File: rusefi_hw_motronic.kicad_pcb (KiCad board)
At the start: 2 copper layers, 175 x 129 mm, 43 parts, among them J1 OMEGA PCC_SMP_K, J2 Conn_01x02_Female, Q1 ZXTN2040, U1 SFH617A-2X009T, U2 BOSCH_55P, U3 molex_48pin_MRE, U4 MAX31855KASA, U5 TPIC8101, U6 MPXA4250A6U, U7 TE_6437288-6

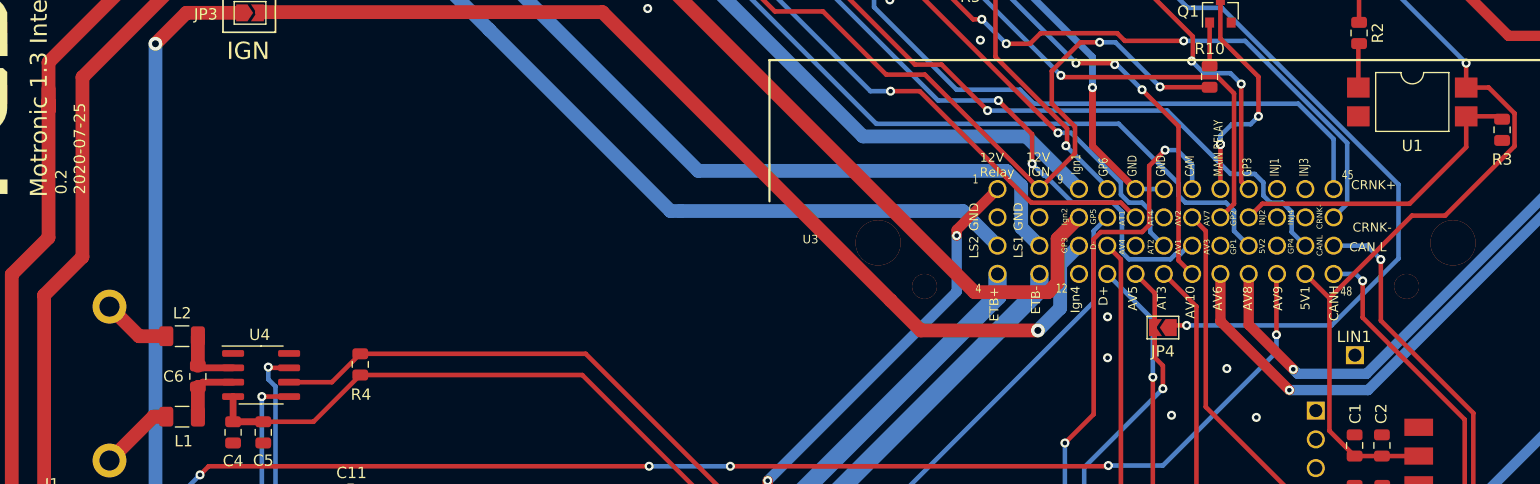
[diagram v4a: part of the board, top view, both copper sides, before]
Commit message: added PPS pins
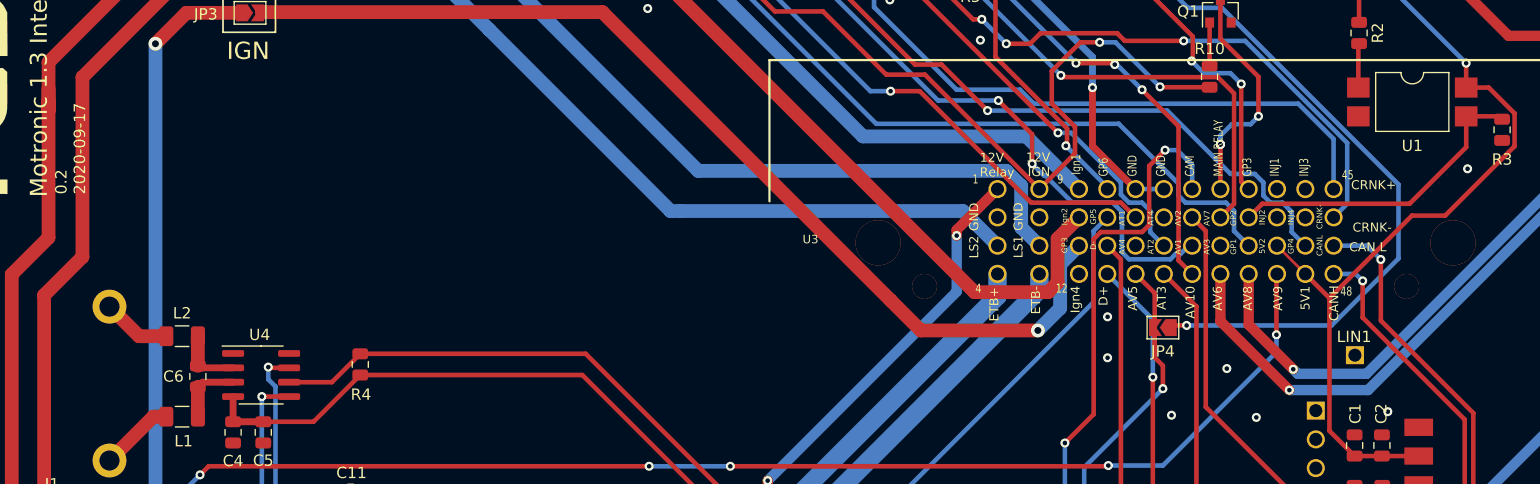
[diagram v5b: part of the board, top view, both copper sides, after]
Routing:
- net +5V: track 277.8 -> 281.3 mm
- net GND: vias 30 -> 32
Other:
- board text added: "0.2 2020-09-17"
- board text removed: "0.2 2020-07-25"

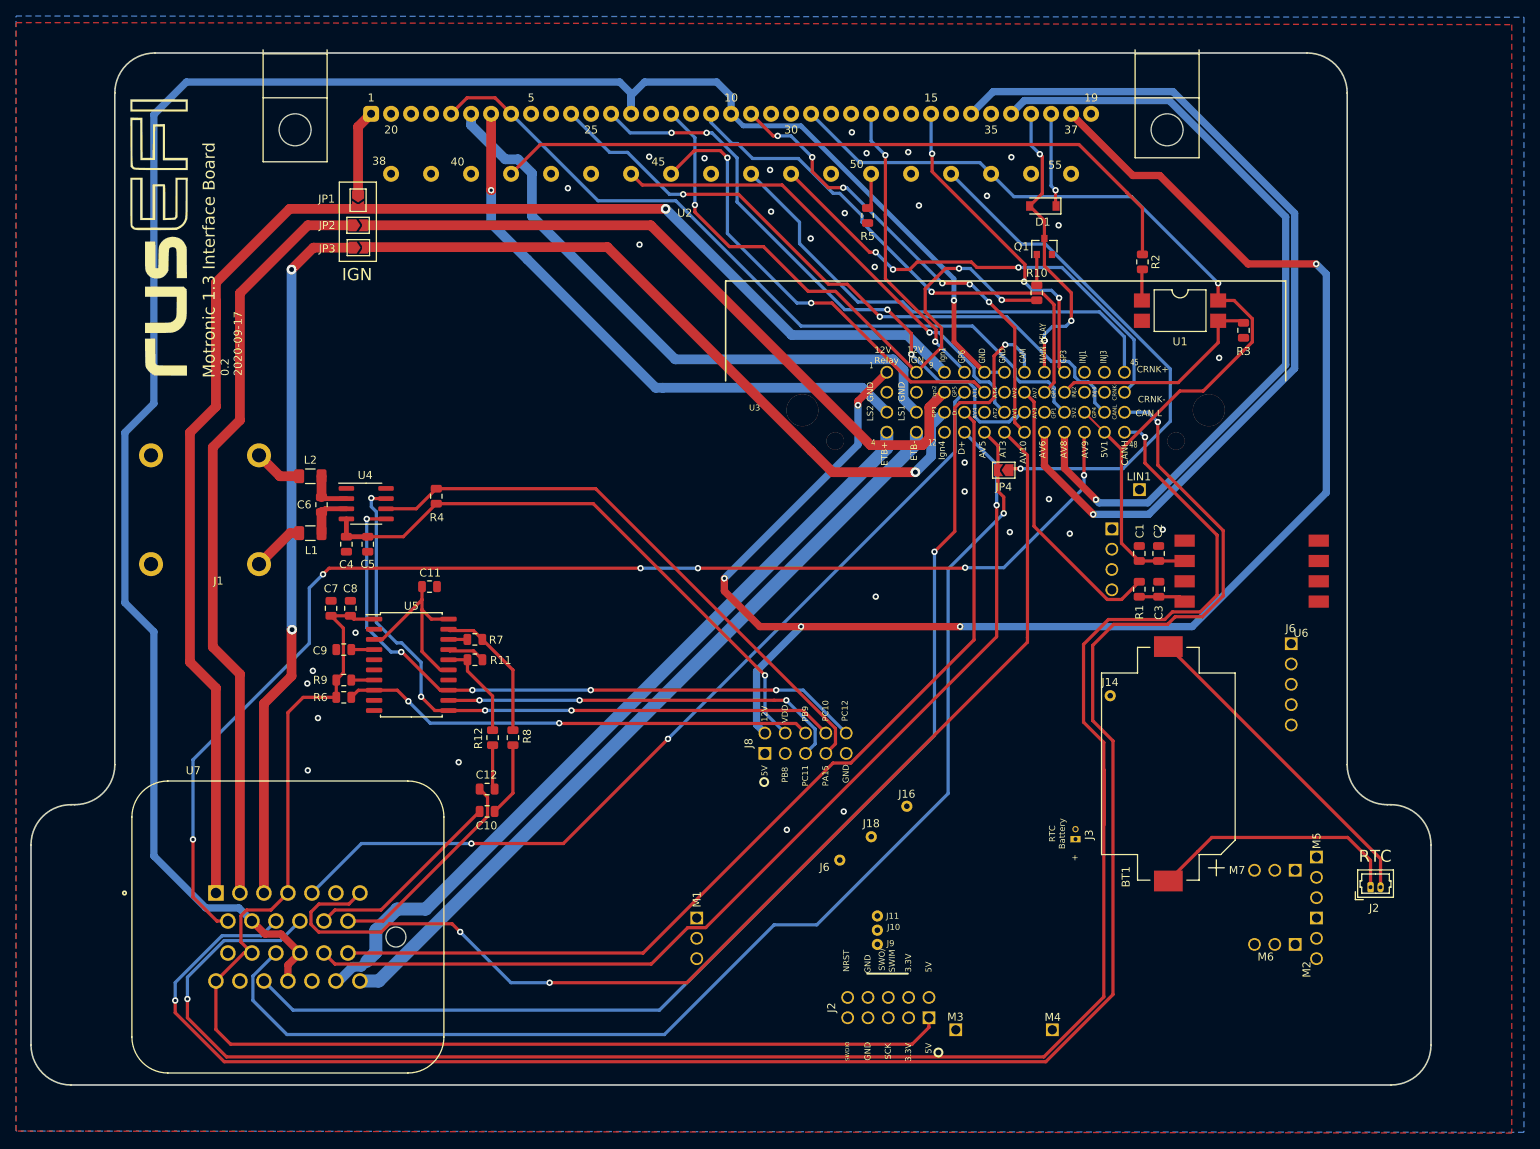
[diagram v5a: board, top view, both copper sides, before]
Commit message: added etb sensor pins to layout
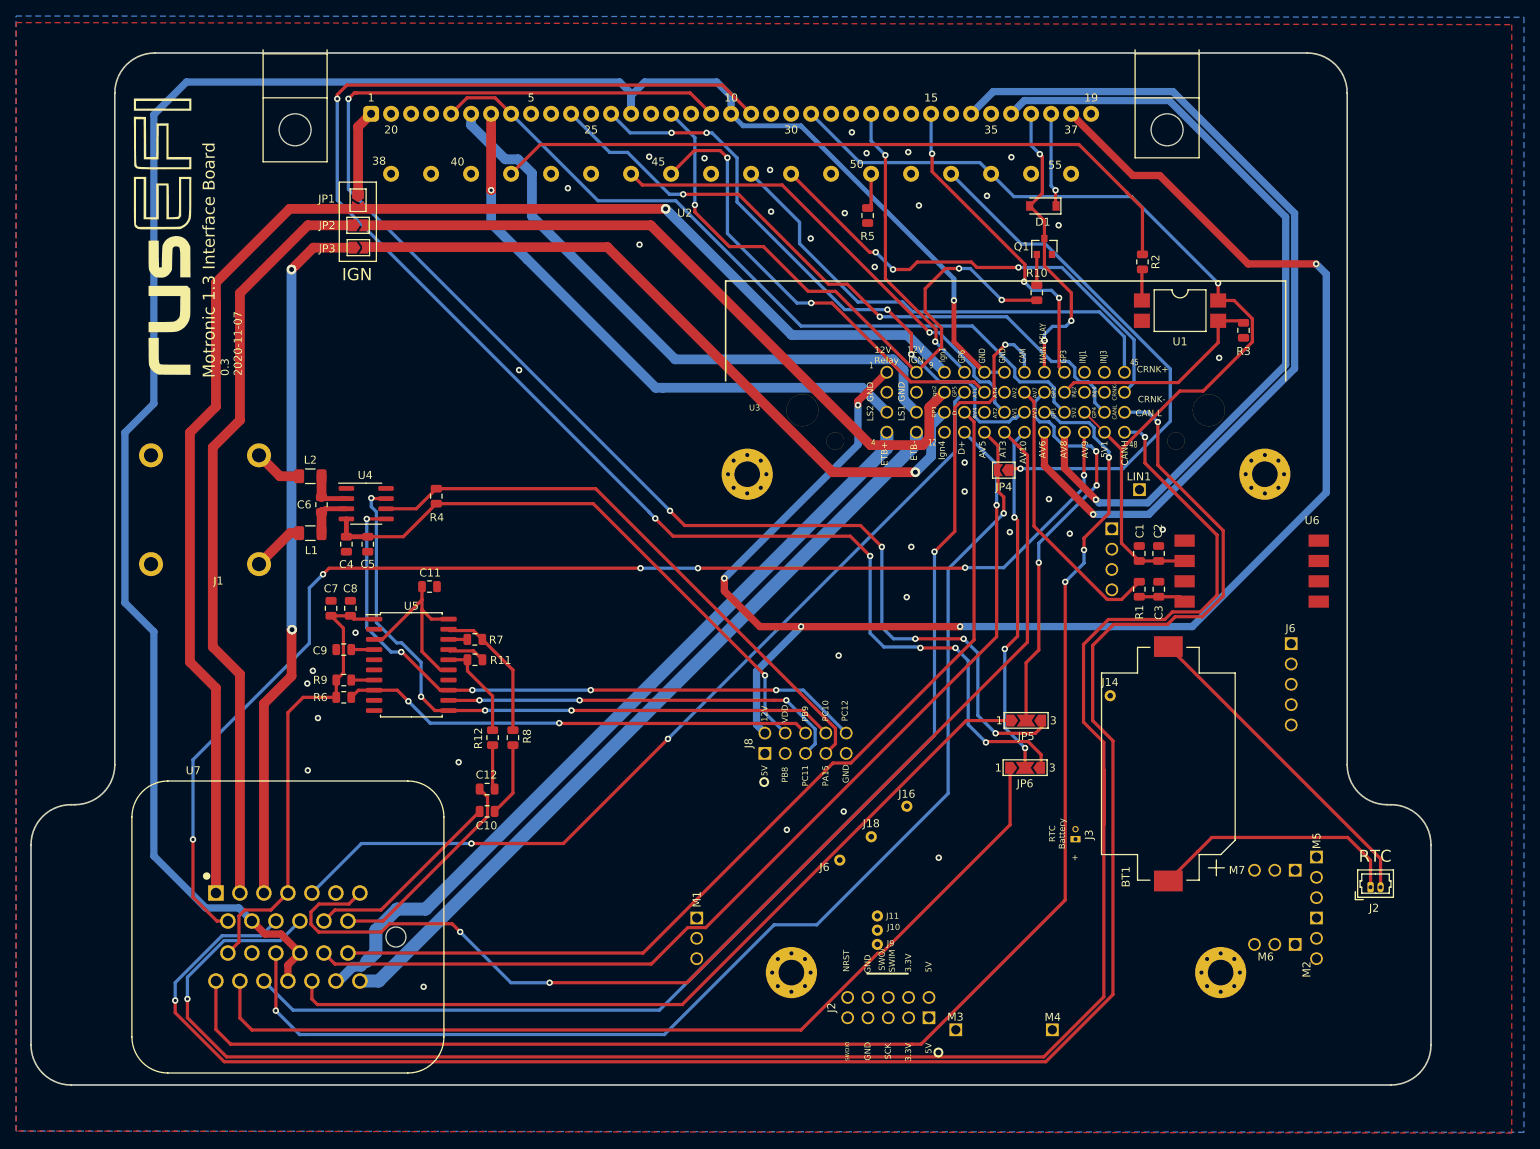
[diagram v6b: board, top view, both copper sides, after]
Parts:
- added JP5: SolderJumper_3_Open, Jumper:SolderJumper-3_P2.0mm_Open_TrianglePad1.0x1.5mm_NumberLabels, F.Cu at (147.6, 111.2)
- added JP6: SolderJumper_3_Open, Jumper:SolderJumper-3_P2.0mm_Open_TrianglePad1.0x1.5mm_NumberLabels, F.Cu at (147.4, 117.1)
- added REF**: MountingHole_3.2mm_M3_Pad_Via, MountingHole:MountingHole_3.2mm_M3_Pad_Via, F.Cu at (118.2, 142.7)
- added REF**: MountingHole_3.2mm_M3_Pad_Via, MountingHole:MountingHole_3.2mm_M3_Pad_Via, F.Cu at (171.9, 142.7)
- added REF**: MountingHole_3.2mm_M3_Pad_Via, MountingHole:MountingHole_3.2mm_M3_Pad_Via, F.Cu at (177.4, 80.4)
- added REF**: MountingHole_3.2mm_M3_Pad_Via, MountingHole:MountingHole_3.2mm_M3_Pad_Via, F.Cu at (112.7, 80.4)
- moved G*** 0.46 mm to (39.6, 50.7)
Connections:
- net TPS renamed TPS1
- U3 pad 28: VEHICLE_SPEED -> AV10
- U3 pad 30: O2_IN -> AV7
- U3 pad 31: Net-(U3-Pad31) -> PPS1
- U7 pad 14: GND -> +5V
- U7 pad 15: +5V -> GND
- U7 pad 20: +5V -> PPS1
- U7 pad 21: GND -> PPS2
- U7 pad 24: Net-(U7-Pad24) -> TPS2
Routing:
- net PPS1: track 0.00 -> 189.5 mm, vias 0 -> 3
- net VEHICLE_SPEED: track 58.6 -> 195.7 mm
- net PPS2: track 0.00 -> 119.3 mm
- net O2_IN: track 65.3 -> 184.4 mm, vias 1 -> 6
- net TPS2: track 0.00 -> 104.5 mm
- net +5V: track 281.3 -> 177.6 mm
- net AV7: track 0.00 -> 51.1 mm, vias 0 -> 3
- net AV10: track 0.00 -> 44.4 mm, vias 0 -> 3
- net TPS1: track 157.3 -> 154.0 mm, vias 1 -> 2
- net GND: vias 32 -> 37
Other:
- board text added: "0.3 2020-11-07"
- board text removed: "0.2 2020-09-17"

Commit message: esp32 schematics
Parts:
- removed G***: LOGO, rusefi_motronic:rusefi_logo
- removed REF** (x4): MountingHole_3.2mm_M3_Pad_Via, MountingHole:MountingHole_3.2mm_M3_Pad_Via
- added U8: ESP32-WROOM-32, RF_Module:ESP32-WROOM-32, F.Cu at (55.9, 65.3)

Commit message: board cleanup
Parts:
- moved JP1 10.2 mm to (74.2, 47.4)
- moved JP2 10.2 mm to (74.2, 50.5)
- moved JP3 10.2 mm to (74.3, 53.3)
- moved C4 1.27 mm to (62.6, 90.4)
- moved C5 1.27 mm to (65.3, 90.4)
- moved C6 1.27 mm to (59.5, 85.5)
- moved L2 1.27 mm to (58.1, 81.9)
- moved J1 1.27 mm to (51.7, 86.1)
- moved L1 1.27 mm to (58.1, 89.0)
- moved R4 1.27 mm to (73.9, 84.4)
- moved U4 1.27 mm to (65.1, 85.3)
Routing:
- net CAM: track 159.2 -> 152.8 mm, vias 2 -> 1
- net Net-(JP1-Pad1): track 10.7 -> 14.9 mm
- net IGN3: track 88.2 -> 84.3 mm
- net O2_IN: track 184.4 -> 187.6 mm
- net VEHICLE_SPEED: track 195.7 -> 198.5 mm
- net CS_EGT: track 73.3 -> 72.7 mm
- net +3V3: track 73.4 -> 72.9 mm
